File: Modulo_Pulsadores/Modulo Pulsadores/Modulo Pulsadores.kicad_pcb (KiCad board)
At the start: 2 copper layers, 43.2 x 43.8 mm, 12 parts, among them J1 Conn_01x06_Female, J2 Conn_01x06_Male, J3 Conn_01x03_Male, J4 Conn_01x03_Male, SW1 SW_Push, SW2 SW_Push, SW3 SW_Push, SW4 SW_Push

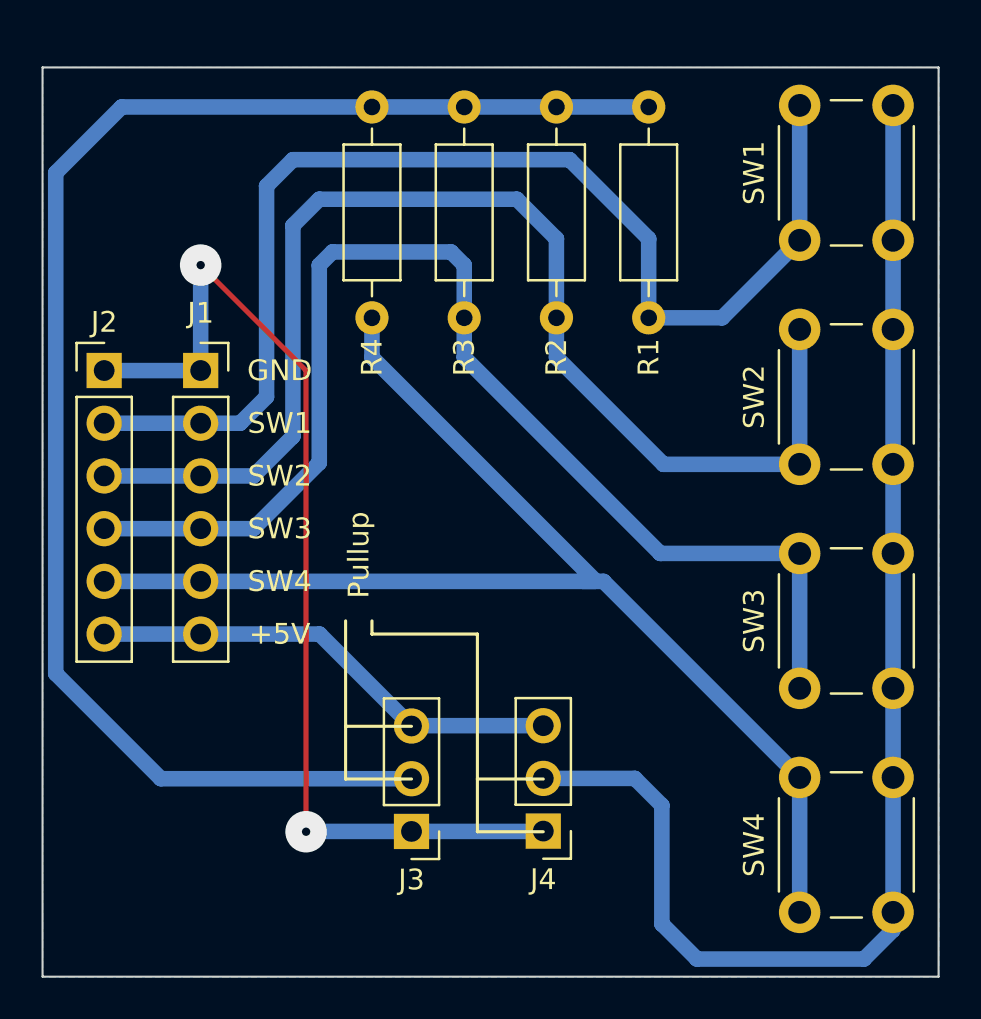
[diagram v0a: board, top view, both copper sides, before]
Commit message: Rerouted Modulo Pulsadores
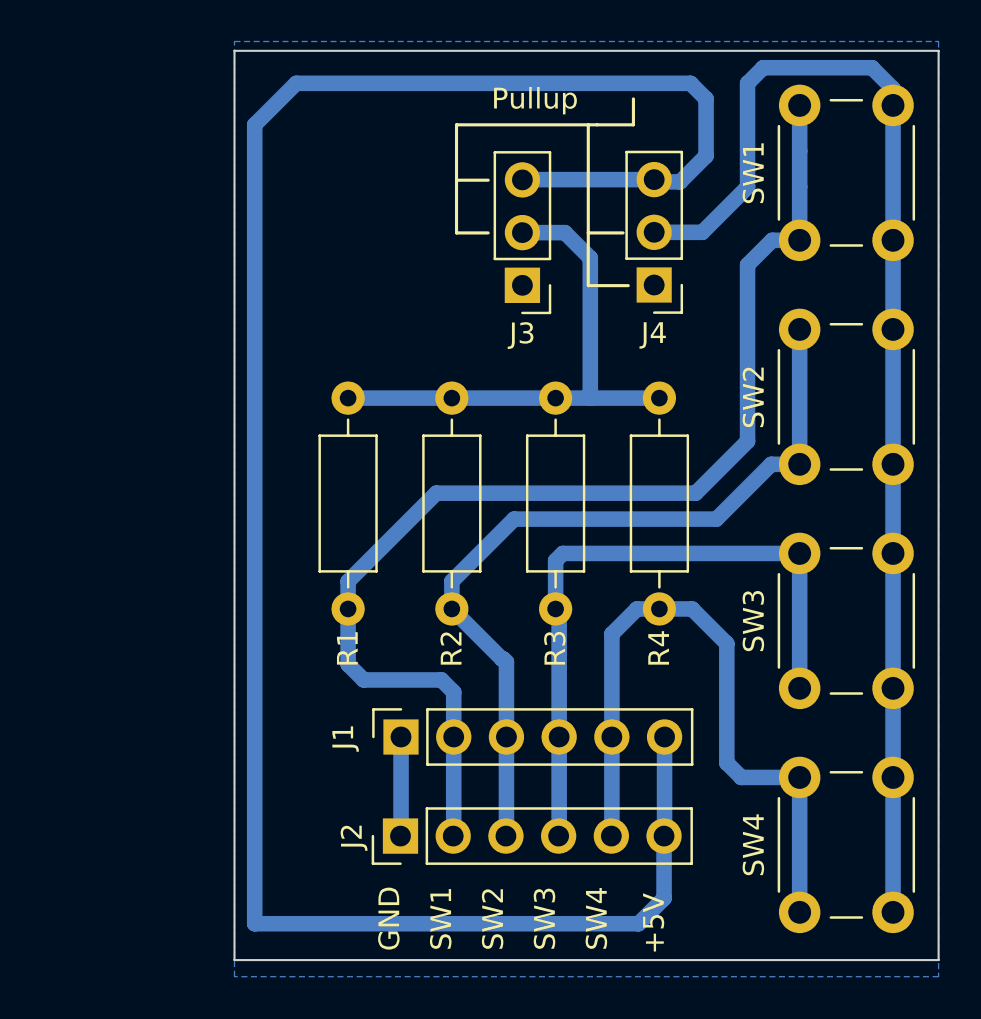
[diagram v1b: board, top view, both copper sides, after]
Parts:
- moved J3 26.9 mm to (96.2, 81.0)
- moved J4 26.9 mm to (102.5, 81.0)
- moved J2 26.6 mm to (90.3, 107.5), turned to 90 degrees
- moved R1 20.2 mm to (87.8, 86.4)
- moved J1 20.1 mm to (90.3, 102.8), turned to 90 degrees
- moved R4 19.7 mm to (102.8, 86.4)
- moved R2 14.9 mm to (92.8, 86.4)
- moved R3 14.7 mm to (97.8, 86.4)
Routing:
- net +5V: track 23.0 -> 101.6 mm
- net Net-(J3-Pad2): track 73.3 -> 25.5 mm
- net GND: track 50.6 -> 4.81 mm, vias 2 -> 0
- net Net-(R4-Pad2): track 61.7 -> 32.5 mm
- net Net-(J1-Pad4): track 59.7 -> 31.8 mm
- net Net-(J1-Pad3): track 60.2 -> 39.0 mm
- net Net-(J4-Pad2): track 64.1 -> 57.8 mm
- net Net-(R1-Pad2): track 58.2 -> 56.6 mm
- added copper zone on B.Cu, net GND
- removed copper zone on B.Cu, net (none)
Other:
- board size 43.2 x 43.8 mm -> 33.9 x 43.8 mm

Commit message: Rerouted Modulo Pulsadores
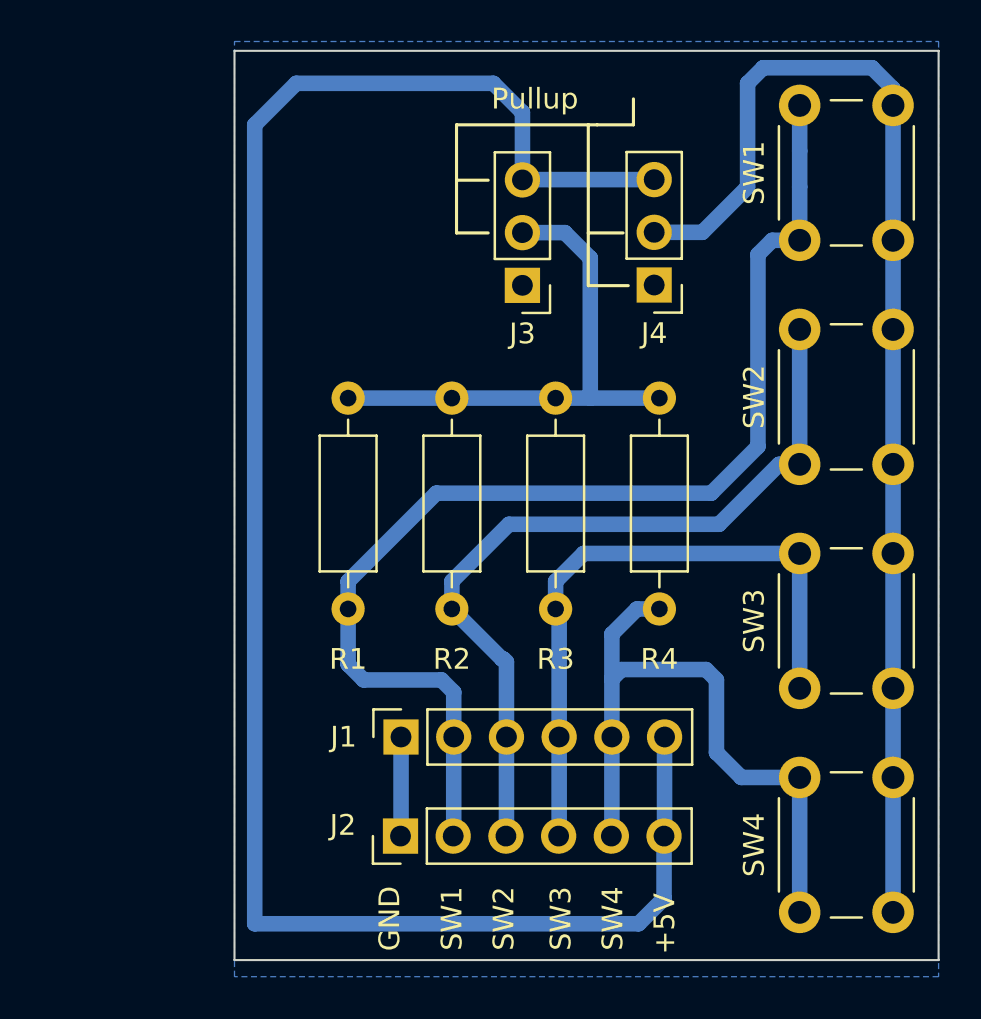
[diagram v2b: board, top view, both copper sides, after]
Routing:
- net +5V: track 101.6 -> 90.6 mm
- net Net-(J1-Pad4): track 31.8 -> 31.2 mm
